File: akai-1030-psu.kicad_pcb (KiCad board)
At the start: 2 copper layers, 110 x 65 mm, 73 parts, among them J1 #1, J10.1 #10.1, J10.2 #10.2, J11.1 #11.1, J11.2 #11.2, J12 #12, J13 #13, J14 #14, J15 #15, J16 30.6VDC, J17 12.2V, J18 #18, J19 #Q3-2, J2 #2, J20 #Q1-2, J3 #3, J4 #4, J5 #5, J6 #6, J7 #7, J8 #8, J9.1 #9.1, J9.2 #9.2, Q1 Q_NPN_BCE, Q2 Q_NPN_ECB, Q3 Q_NPN_BCE

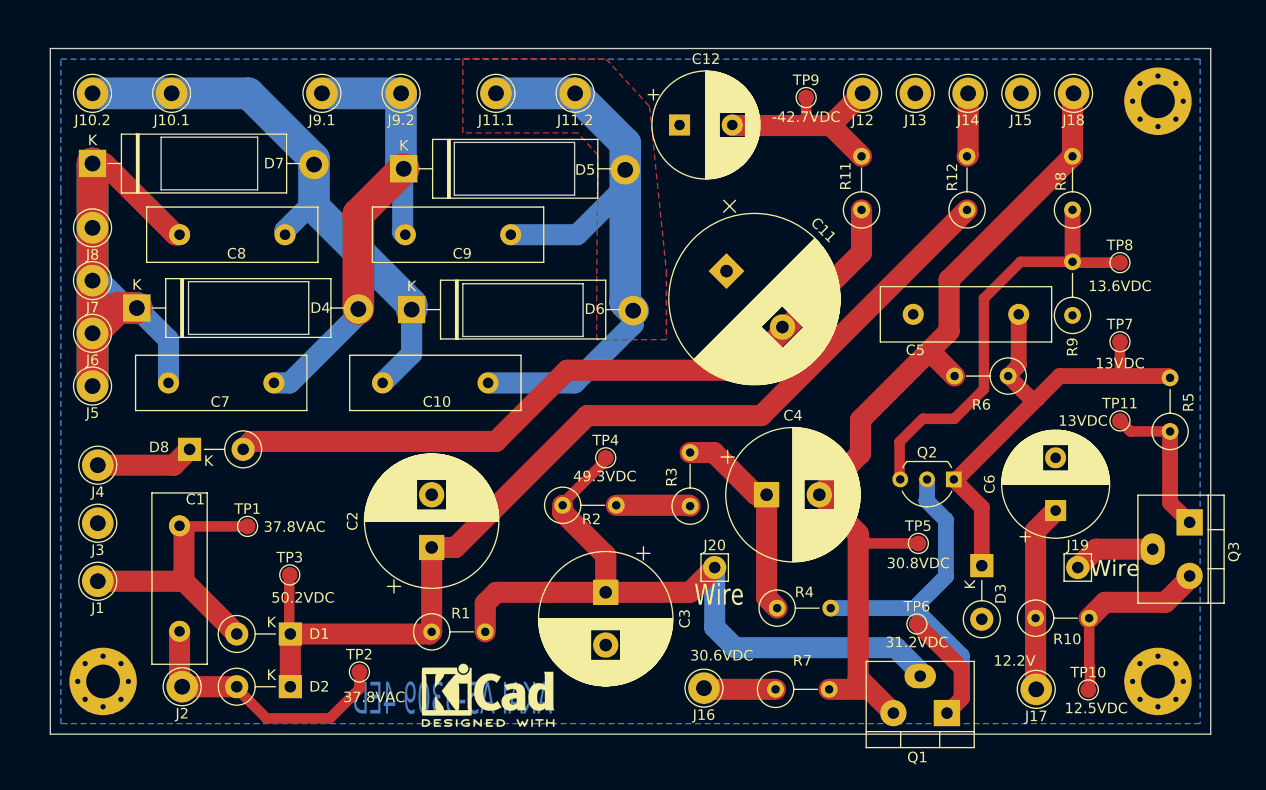
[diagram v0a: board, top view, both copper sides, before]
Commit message: Make revision B.
- Give some space to J16 and J17 for easier mounting.
- Move lower caps to the left
- Move annotations
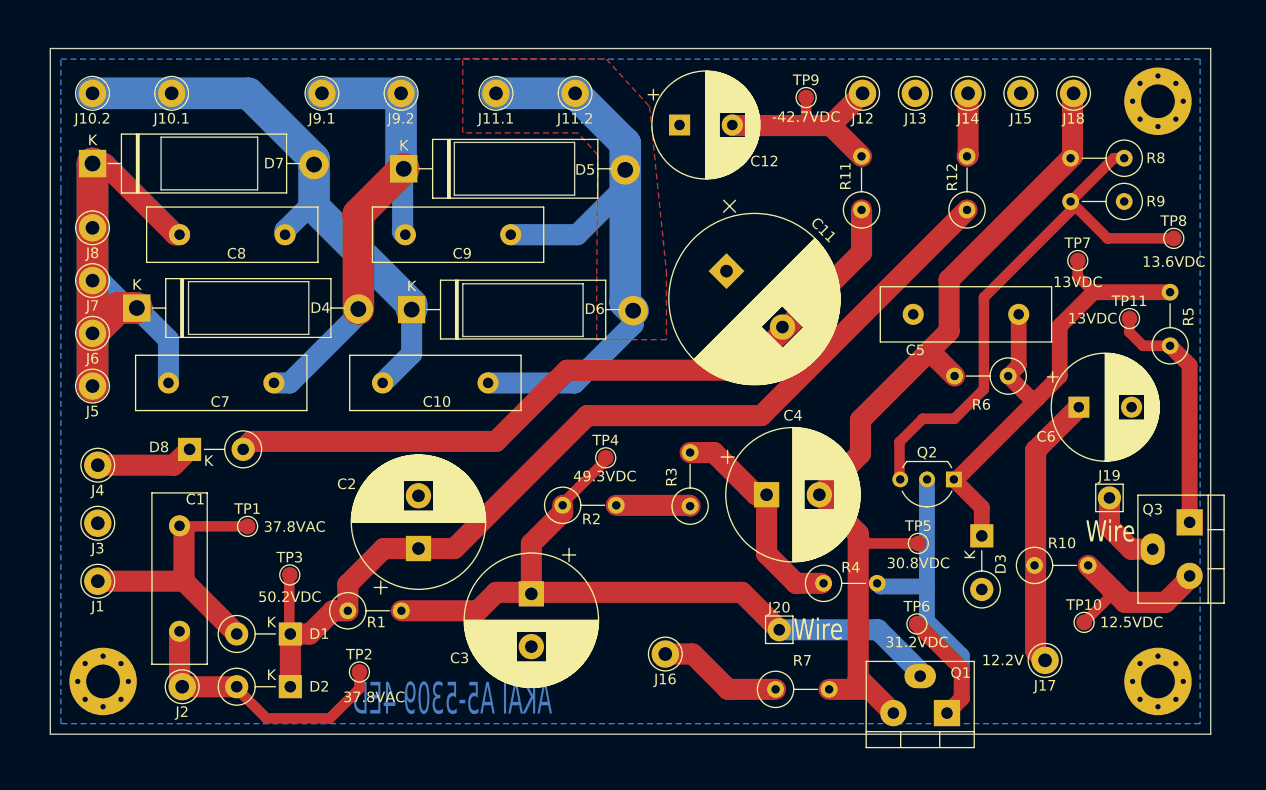
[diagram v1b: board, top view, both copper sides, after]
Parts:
- removed REF**: KiCad-Logo2_5mm_SilkScreen, Symbol:KiCad-Logo2_5mm_SilkScreen
- J1, J10.1, J10.2, J11.1, J11.2, J12, J13, J14, J15, J16, J17, J18, J2, J3, J4, J5, J6, J7, J8, J9.1, J9.2: footprint Connector_Pin:Pin_D1.3mm_L11.0mm_LooseFit -> Connector_Pin:Pin_D1.3mm_L11.0mm
- moved R9 11.9 mm to (170.9, 70.2), turned to 180 degrees
- moved C6 10.0 mm to (166.6, 89.7), turned to 0 degrees
- moved TP11 9.74 mm to (171.4, 81.3)
- moved TP7 8.68 mm to (166.5, 75.8)
- moved J20 8.50 mm to (138.2, 110.8)
- moved R1 8.20 mm to (97.3, 109.0)
- moved R5 8.12 mm to (175.2, 83.9)
- moved J19 7.25 mm to (169.5, 98.3)
- moved C3 7.05 mm to (114.7, 107.4)
- moved R8 6.93 mm to (170.9, 66.1), turned to 180 degrees
- moved TP10 6.41 mm to (167.1, 110.1)
- moved TP8 5.59 mm to (175.6, 73.7)
- moved R10 5.00 mm to (162.4, 104.7)
- moved R4 4.99 mm to (142.4, 106.4)
- moved J16 4.89 mm to (127.4, 113.1)
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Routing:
- net Net-(Q2-Pad3): track 41.5 -> 52.9 mm
- net Net-(Q3-Pad1): track 14.6 -> 23.2 mm
- net Net-(C6-Pad1): track 17.8 -> 26.1 mm
- net Net-(Q1-Pad1): track 45.3 -> 39.7 mm
- net Net-(J16-Pad1): track 6.83 -> 11.8 mm
- net Net-(C5-Pad1): track 47.1 -> 50.6 mm
- net Net-(C2-Pad1): track 96.0 -> 92.8 mm
- net Net-(Q3-Pad3): track 18.0 -> 16.3 mm
- net Net-(C4-Pad1): track 20.1 -> 20.9 mm

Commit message: Add model name
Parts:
- moved TP6 11.9 mm to (160.3, 117.9)
- moved J20 4.10 mm to (142.3, 110.8)
- moved C11 2.79 mm to (134.2, 79.4), turned to 0 degrees
- moved TP5 2.70 mm to (149.3, 100.9)
- moved D3 2.47 mm to (158.0, 99.5)
- moved J17 2.33 mm to (162.4, 111.6)
- moved C12 1.67 mm to (128.5, 61.3)
- moved TP3 1.02 mm to (90.8, 105.8)
- moved R4 0.62 mm to (143.0, 106.4)
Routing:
- net Net-(C7-Pad1): track 83.2 -> 42.3 mm
- net Net-(Q1-Pad1): track 39.7 -> 32.9 mm
- net Net-(C7-Pad2): track 47.6 -> 41.1 mm
- net Net-(C10-Pad1): track 57.6 -> 53.2 mm
- net Net-(C6-Pad1): track 26.1 -> 23.5 mm
- net Net-(C4-Pad2): track 85.2 -> 82.8 mm
- net Net-(C5-Pad1): track 50.6 -> 48.3 mm
- net Net-(C10-Pad2): track 62.1 -> 63.4 mm
- net Net-(C12-Pad2): track 20.5 -> 21.4 mm
- net Net-(C1-Pad2): track 26.8 -> 26.1 mm
- removed copper zone on F.Cu, net Net-(C10-Pad2)
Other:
- net class Default removed
